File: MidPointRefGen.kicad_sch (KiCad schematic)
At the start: 27 parts, among them SW10 SW_SPDT, SW11 SW_SPDT, U2 BUF634A, U3 OPA191, U4 OPA191

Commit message: minor schematic changes, 4 way dip now used instead of 6. switch and pot footprints and symbols done
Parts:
- removed U3, U4: OPA191, Package_TO_SOT_SMD:SOT-23, symbol uniOpAmpLib:OPA191
- added U3, U4: OPA992DBV, Package_TO_SOT_SMD:SOT-23-5_HandSoldering, symbol uniOpAmpLib:OPA992DBV
- renumbered RN1 to RN2, SW10 to SW14, SW11 to SW15
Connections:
- net +VDC: now also U3.5 (V+), U4.5 (V+)
- net -VDC: now also U3.2 (V-), U4.2 (V-)
- net at R5.1: now also U4.1
- net at SW14.2 (B): now also U3.3 (+), U4.3 (+)
- net at R2.1: now also U4.4 (-)
- net at R1.2: now also U3.4 (-)
- net at R3.2: now also U3.1
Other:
- moved on the sheet: C17, C18, C19

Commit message: Initial PCB layout
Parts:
- renumbered C11 to C10, C12 to C11, C13 to C12, C14 to C13, C15 to C14, C16 to C15, C17 to C16, C18 to C17, C19 to C18, C20 to C19, C21 to C20, C22 to C21, C23 to C22, C24 to C23, C25 to C24, SW15 to SW10, SW14 to SW9
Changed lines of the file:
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@@
 		(dnp no)
 		(fields_autoplaced yes)
-		(property "Reference" "C16"
+		(property "Reference" "C15"
 			(at 62.23 170.1799 0)
 			(show_name no)
@@
 			(project "universalOpAmpV0"
 				(path "/0c9d5097-e341-4aa8-a29f-4bc5e653f52f/5d62f848-01bc-4b5b-b6c6-edef66e267d0"
-					(reference "C16")
+					(reference "C15")
 					(unit 1)
 				)
@@
 		(dnp no)
 		(fields_autoplaced yes)
-		(property "Reference" "C23"
+		(property "Reference" "C22"
 			(at 207.01 63.4999 0)
 			(show_name no)
@@
 			(project "universalOpAmpV0"
 				(path "/0c9d5097-e341-4aa8-a29f-4bc5e653f52f/5d62f848-01bc-4b5b-b6c6-edef66e267d0"
-					(reference "C23")
+					(reference "C22")
 					(unit 1)
 				)
@@
 		(dnp no)
 		(fields_autoplaced yes)
-		(property "Reference" "C14"
+		(property "Reference" "C13"
 			(at 52.07 170.1799 0)
 			(show_name no)
@@
 			(project "universalOpAmpV0"
 				(path "/0c9d5097-e341-4aa8-a29f-4bc5e653f52f/5d62f848-01bc-4b5b-b6c6-edef66e267d0"
-					(reference "C14")
+					(reference "C13")
 					(unit 1)
 				)
@@
 		(dnp no)
 		(fields_autoplaced yes)
-		(property "Reference" "C25"
+		(property "Reference" "C24"
 			(at 217.17 63.4999 0)
 			(show_name no)
@@
 			(project "universalOpAmpV0"
 				(path "/0c9d5097-e341-4aa8-a29f-4bc5e653f52f/5d62f848-01bc-4b5b-b6c6-edef66e267d0"
-					(reference "C25")
+					(reference "C24")
 					(unit 1)
 				)
@@
 		(dnp no)
 		(fields_autoplaced yes)
-		(property "Reference" "C22"
+		(property "Reference" "C21"
 			(at 207.01 55.8799 0)
 			(show_name no)
@@
 			(project "universalOpAmpV0"
 				(path "/0c9d5097-e341-4aa8-a29f-4bc5e653f52f/5d62f848-01bc-4b5b-b6c6-edef66e267d0"
-					(reference "C22")
+					(reference "C21")
 					(unit 1)
 				)
@@
 		(in_pos_files yes)
 		(dnp no)
-		(property "Reference" "C19"
+		(property "Reference" "C18"
 			(at 154.94 169.2909 0)
 			(show_name no)
@@
 			(project "universalOpAmpV0"
 				(path "/0c9d5097-e341-4aa8-a29f-4bc5e653f52f/5d62f848-01bc-4b5b-b6c6-edef66e267d0"
-					(reference "C19")
+					(reference "C18")
 					(unit 1)
 				)
@@
 		(dnp no)
 		(fields_autoplaced yes)
-		(property "Reference" "SW14"
+		(property "Reference" "SW9"
 			(at 73.66 69.85 0)
 			(show_name no)
@@
 			(project "universalOpAmpV0"
 				(path "/0c9d5097-e341-4aa8-a29f-4bc5e653f52f/5d62f848-01bc-4b5b-b6c6-edef66e267d0"
-					(reference "SW14")
+					(reference "SW9")
 					(unit 1)
 				)
@@
 		(in_pos_files yes)
 		(dnp no)
-		(property "Reference" "C11"
+		(property "Reference" "C10"
 			(at 34.29 123.5709 0)
 			(show_name no)
@@
 			(project "universalOpAmpV0"
 				(path "/0c9d5097-e341-4aa8-a29f-4bc5e653f52f/5d62f848-01bc-4b5b-b6c6-edef66e267d0"
-					(reference "C11")
+					(reference "C10")
 					(unit 1)
 				)
@@
 		(dnp no)
 		(fields_autoplaced yes)
-		(property "Reference" "C24"
+		(property "Reference" "C23"
 			(at 217.17 55.8799 0)
 			(show_name no)
@@
 			(project "universalOpAmpV0"
 				(path "/0c9d5097-e341-4aa8-a29f-4bc5e653f52f/5d62f848-01bc-4b5b-b6c6-edef66e267d0"
-					(reference "C24")
+					(reference "C23")
 					(unit 1)
 				)
@@
 		(dnp no)
 		(fields_autoplaced yes)
-		(property "Reference" "C13"
+		(property "Reference" "C12"
 			(at 52.07 124.4599 0)
 			(show_name no)
@@
 			(project "universalOpAmpV0"
 				(path "/0c9d5097-e341-4aa8-a29f-4bc5e653f52f/5d62f848-01bc-4b5b-b6c6-edef66e267d0"
-					(reference "C13")
+					(reference "C12")
 					(unit 1)
 				)
@@
 		(in_pos_files yes)
 		(dnp no)
-		(property "Reference" "C12"
+		(property "Reference" "C11"
 			(at 34.29 169.2909 0)
 			(show_name no)
@@
 			(project "universalOpAmpV0"
 				(path "/0c9d5097-e341-4aa8-a29f-4bc5e653f52f/5d62f848-01bc-4b5b-b6c6-edef66e267d0"
-					(reference "C12")
+					(reference "C11")
 					(unit 1)
 				)
@@
 		(dnp no)
 		(fields_autoplaced yes)
-		(property "Reference" "SW15"
+		(property "Reference" "SW10"
 			(at 163.83 52.07 0)
 			(show_name no)
@@
 			(project "universalOpAmpV0"
 				(path "/0c9d5097-e341-4aa8-a29f-4bc5e653f52f/5d62f848-01bc-4b5b-b6c6-edef66e267d0"
-					(reference "SW15")
+					(reference "SW10")
 					(unit 1)
 				)
@@
 		(in_pos_files yes)
 		(dnp no)
-		(property "Reference" "C20"
+		(property "Reference" "C19"
 			(at 189.23 54.9909 0)
 			(show_name no)
@@
 			(project "universalOpAmpV0"
 				(path "/0c9d5097-e341-4aa8-a29f-4bc5e653f52f/5d62f848-01bc-4b5b-b6c6-edef66e267d0"
-					(reference "C20")
+					(reference "C19")
 					(unit 1)
 				)
@@
 		(dnp no)
 		(fields_autoplaced yes)
-		(property "Reference" "C17"
+		(property "Reference" "C16"
 			(at 127 170.1799 0)
 			(show_name no)
@@
 			(project "universalOpAmpV0"
 				(path "/0c9d5097-e341-4aa8-a29f-4bc5e653f52f/5d62f848-01bc-4b5b-b6c6-edef66e267d0"
-					(reference "C17")
+					(reference "C16")
 					(unit 1)
 				)
@@
 		(dnp no)
 		(fields_autoplaced yes)
-		(property "Reference" "C15"
+		(property "Reference" "C14"
 			(at 62.23 124.4599 0)
 			(show_name no)
@@
 			(project "universalOpAmpV0"
 				(path "/0c9d5097-e341-4aa8-a29f-4bc5e653f52f/5d62f848-01bc-4b5b-b6c6-edef66e267d0"
-					(reference "C15")
+					(reference "C14")
 					(unit 1)
 				)
@@
 		(dnp no)
 		(fields_autoplaced yes)
-		(property "Reference" "C18"
+		(property "Reference" "C17"
 			(at 137.16 170.1799 0)
 			(show_name no)
@@
 			(project "universalOpAmpV0"
 				(path "/0c9d5097-e341-4aa8-a29f-4bc5e653f52f/5d62f848-01bc-4b5b-b6c6-edef66e267d0"
-					(reference "C18")
+					(reference "C17")
 					(unit 1)
 				)
@@
 		(in_pos_files yes)
 		(dnp no)
-		(property "Reference" "C21"
+		(property "Reference" "C20"
 			(at 189.23 62.6109 0)
 			(show_name no)
@@
 			(project "universalOpAmpV0"
 				(path "/0c9d5097-e341-4aa8-a29f-4bc5e653f52f/5d62f848-01bc-4b5b-b6c6-edef66e267d0"
-					(reference "C21")
+					(reference "C20")
 					(unit 1)
 				)

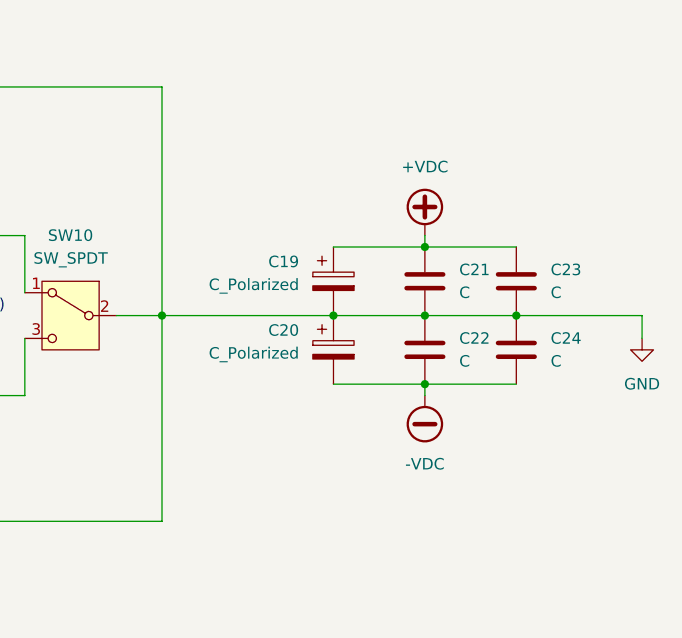
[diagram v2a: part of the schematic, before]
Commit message: oops scope creep - now there is a frequency counter
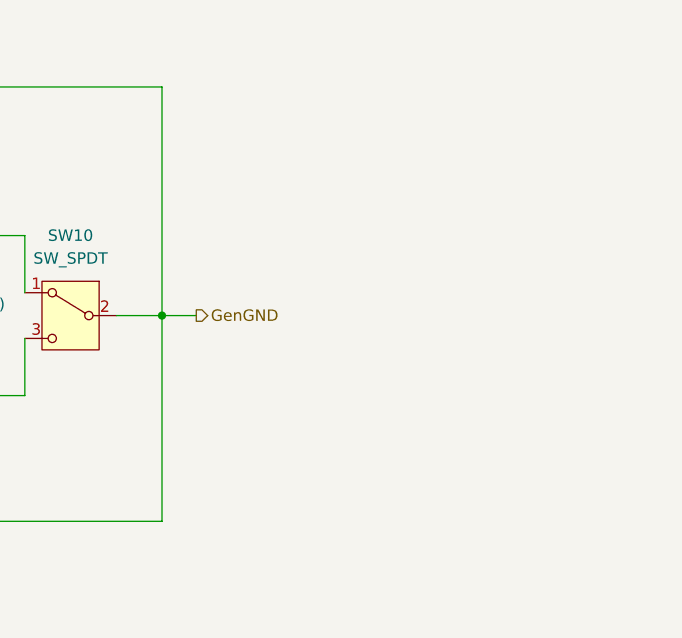
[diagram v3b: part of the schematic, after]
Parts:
- removed C19, C20: C_Polarized, symbol Device:C_Polarized
- removed C21, C22, C23, C24: C, symbol Device:C
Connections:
- net GND renamed GenGND

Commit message: Input and output routing complete
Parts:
- removed SW10, SW9: SW_SPDT, symbol Switch:SW_SPDT
- added R30: R, Resistor_SMD:R_0805_2012Metric_Pad1.20x1.40mm_HandSolder, symbol Device:R
- added SW9: SW_DPDT_x2, uniOpAmpLib:CAS-DxxB, symbol Switch:SW_DPDT_x2
- R1, R2, R3: footprint (none) -> Resistor_SMD:R_0805_2012Metric_Pad1.20x1.40mm_HandSolder
- R4, R5: footprint (none) -> Resistor_SMD:R_2512_6332Metric_Pad1.40x3.35mm_HandSolder
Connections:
- net -VDC: now also R30.2
- net GenGND: now also SW9.5 (B)
- net at RV3.2: now also SW9.3 (C)
- net at RN2.2: now also SW9.1 (A)
- net at U3.3 (+), U4.3 (+): now also SW9.2 (B)
- net at U2.1 (BW): now also R30.1
- net at R4.1: now also SW9.6 (C)
- net at R5.2: now also SW9.4 (A)

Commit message: Voltage controlled current output circuit and preliminary layout added
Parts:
- C12, C13, C14, C15, C16, C17: footprint (none) -> Capacitor_SMD:C_0805_2012Metric_Pad1.18x1.45mm_HandSolder
- RV3: footprint (none) -> uniOpAmpLib:PVG5H
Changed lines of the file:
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@@
 			)
 		)
-		(property "Footprint" ""
+		(property "Footprint" "Capacitor_SMD:C_0805_2012Metric_Pad1.18x1.45mm_HandSolder"
 			(at 59.3852 175.26 0)
 			(hide yes)
@@
 			)
 		)
-		(property "Footprint" ""
+		(property "Footprint" "uniOpAmpLib:PVG5H"
 			(at 50.8 50.8 0)
 			(hide yes)
@@
 			)
 		)
-		(property "Footprint" ""
+		(property "Footprint" "Capacitor_SMD:C_0805_2012Metric_Pad1.18x1.45mm_HandSolder"
 			(at 49.2252 175.26 0)
 			(hide yes)
@@
 			)
 		)
-		(property "Footprint" ""
+		(property "Footprint" "Capacitor_SMD:C_0805_2012Metric_Pad1.18x1.45mm_HandSolder"
 			(at 49.2252 129.54 0)
 			(hide yes)
@@
 			)
 		)
-		(property "Footprint" ""
+		(property "Footprint" "Capacitor_SMD:C_0805_2012Metric_Pad1.18x1.45mm_HandSolder"
 			(at 129.8448 175.26 0)
 			(hide yes)
@@
 			)
 		)
-		(property "Footprint" ""
+		(property "Footprint" "Capacitor_SMD:C_0805_2012Metric_Pad1.18x1.45mm_HandSolder"
 			(at 59.3852 129.54 0)
 			(hide yes)
@@
 			)
 		)
-		(property "Footprint" ""
+		(property "Footprint" "Capacitor_SMD:C_0805_2012Metric_Pad1.18x1.45mm_HandSolder"
 			(at 140.0048 175.26 0)
 			(hide yes)
